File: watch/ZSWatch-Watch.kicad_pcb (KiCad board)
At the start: 4 copper layers, 41 x 37.5 mm, 64 parts, among them IC401 nPM1300-QEXX, IC501 APDS-9306-065, IC502 BMI270, IC503 LIS2MDLTR, IC504 BMP581, IC505 DRV2603RUNT, IC506 PCA9306JK, IC507 RV-8263-C8, IC601 FAN5622SX, IC602 USBLC6-2P6, IC603 MX25U51245GZ4I00, IC604 NTS0104GU12, M601 NORA-B106, X402 Battery, X509 Motor, X603 Device, X608 Display, X701 MB1, X702 MB2

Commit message: Change to a larger battery connector (JST 1.25). Add pads for speaker instead.
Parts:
- removed LS801: Speaker, Same Sky:CMR-12062S-67
- removed X402: Battery, Connector_JST:JST_SH_SM02B-SRSS-TB_1x02-1MP_P1.00mm_Horizontal
- added J1: 53261-0271, ZSWatch:molex_pico, F.Cu at (188.9, 145.7)
- added TP1: TestPoint, TestPoint:TestPoint_Loop_D3.50mm_Drill0.9mm_Beaded, F.Cu at (186.5, 142.6)
- added TP2: TestPoint_2Pole, TestPoint:TestPoint_2Pads_Pitch2.54mm_Drill0.8mm, F.Cu at (189.7, 138.9)
- added TP3: TestPoint, TestPoint:TestPoint_Loop_D3.50mm_Drill0.9mm_Beaded, F.Cu at (186.5, 148.8)
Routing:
- net /Project Architecture/Peripherals/VBAT: track 54.7 -> 63.2 mm
- net Net-(X702-Pin_3): track 21.3 -> 23.5 mm, vias 1 -> 0
- net GND: track 80.2 -> 82.2 mm
- net Net-(X702-Pin_1): track 19.8 -> 19.5 mm, vias 1 -> 0
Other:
- outline, holes or cut-outs redrawn
- board text added: "+"
- board text added: "-"
- board text added: "GND"
- board text added: "Speaker"
- board text added: "VBAT"

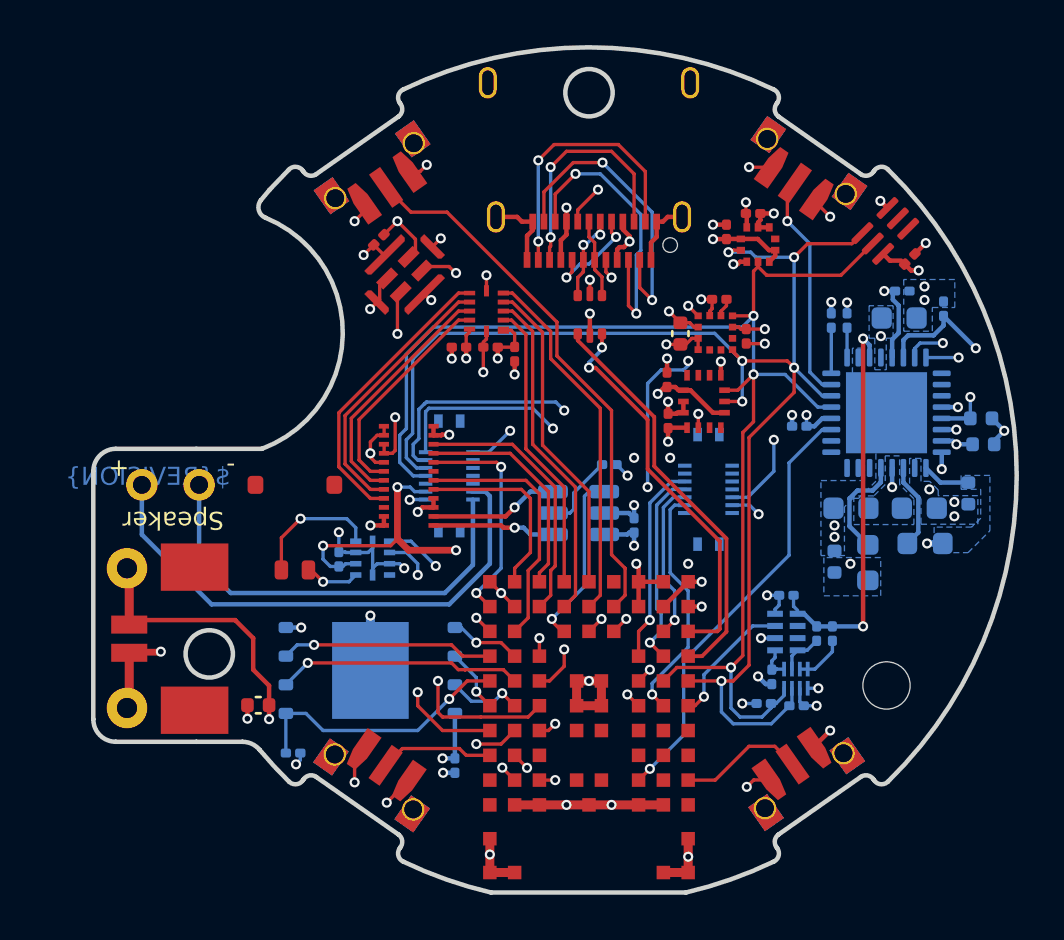
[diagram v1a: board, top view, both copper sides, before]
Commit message: Make battery/speaker stickout 0.5mm shorter. Add few extra Test Points for power at bottom.
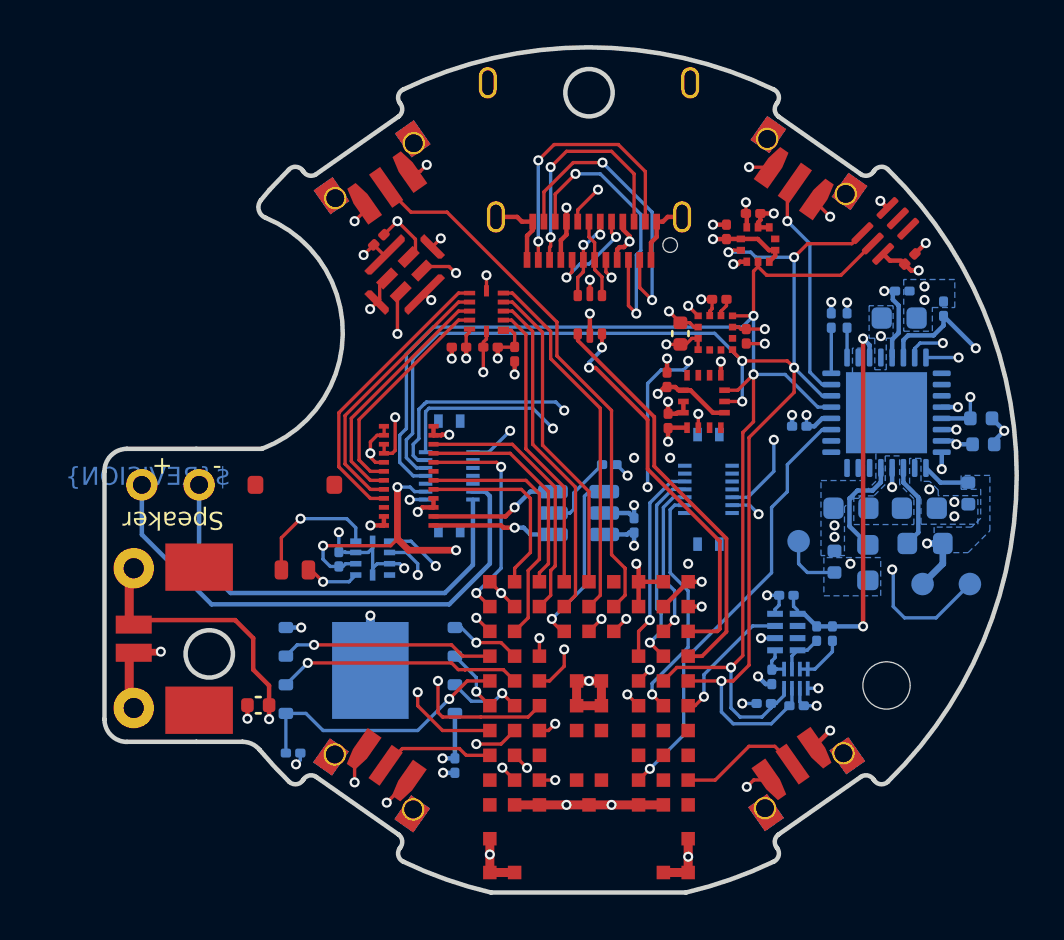
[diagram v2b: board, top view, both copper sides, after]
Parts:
- added TP4: TestPoint, TestPoint:TestPoint_Pad_D1.0mm, B.Cu at (221.8, 143.3)
- added TP5: TestPoint, TestPoint:TestPoint_Pad_D1.0mm, B.Cu at (216.3, 141.4)
- added TP6: TestPoint, TestPoint:TestPoint_Pad_D1.0mm, B.Cu at (223.9, 143.3)
- moved TP1 0.30 mm to (186.8, 142.6)
- moved TP3 0.30 mm to (186.8, 148.8)
- moved J1 0.20 mm to (189.1, 145.7)
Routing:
- net /Project Architecture/Power Management/VSYS: track 59.2 -> 65.1 mm, vias 7 -> 8
- net +3V0: track 47.7 -> 50.5 mm
- net +1V8: track 31.2 -> 33.4 mm
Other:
- board size 41 x 37.5 mm -> 40.5 x 37.5 mm
- board text added: "1V8"
- board text added: "3V0"
- board text added: "NOTE: The speaker will not be soldered by default."
- board text added: "VSYS"
- board text removed: "NOTE: The speaker will not be soldered. Instead the connections is pressure based which allows us to move the pins from the battery connector under the speaker"

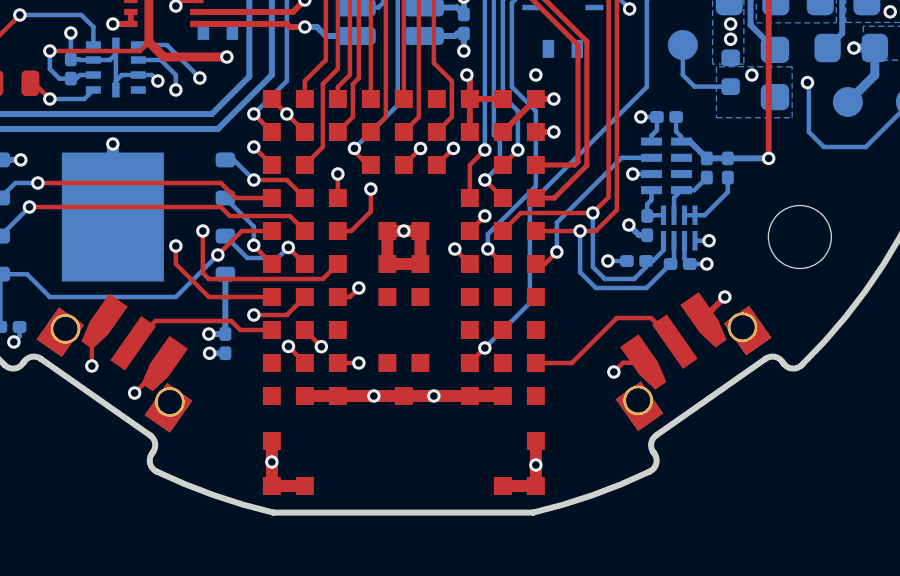
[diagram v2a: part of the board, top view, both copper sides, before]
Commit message: Add test pads for FEM pins if NORA-126 is used instead.
NORA-W126 is a drop in compatible module with FEM to increase output power.
Litterary just to mount this instead of NORA-B106.
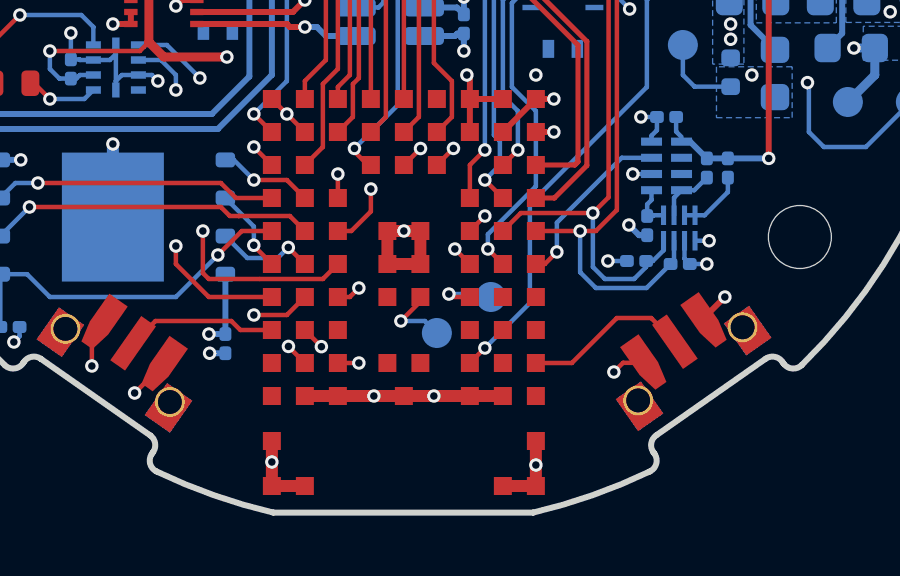
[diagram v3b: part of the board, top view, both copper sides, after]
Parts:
- added TP7: TestPoint, TestPoint:TestPoint_Pad_D1.0mm, B.Cu at (209.9, 149.8)
- added TP8: TestPoint, TestPoint:TestPoint_Pad_D1.0mm, B.Cu at (208.1, 151.0)
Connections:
- M601 pad G5: unconnected-(M601C-P1.08-PadG5) -> Net-(M601C-P1.08)
- M601 pad G7: unconnected-(M601C-P1.09-PadG7) -> Net-(M601C-P1.09)
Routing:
- net Net-(M601C-P1.08): track 0.00 -> 2.43 mm, vias 0 -> 1
- net Net-(M601C-P1.09): track 0.00 -> 2.18 mm, vias 0 -> 1
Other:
- board text added: "P1.08"
- board text added: "P1.09"
